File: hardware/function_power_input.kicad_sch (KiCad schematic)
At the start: 20 parts, among them J5 Conn_01x03_Socket, J6 Conn_01x03_Socket, U3 AZ1117-3.3

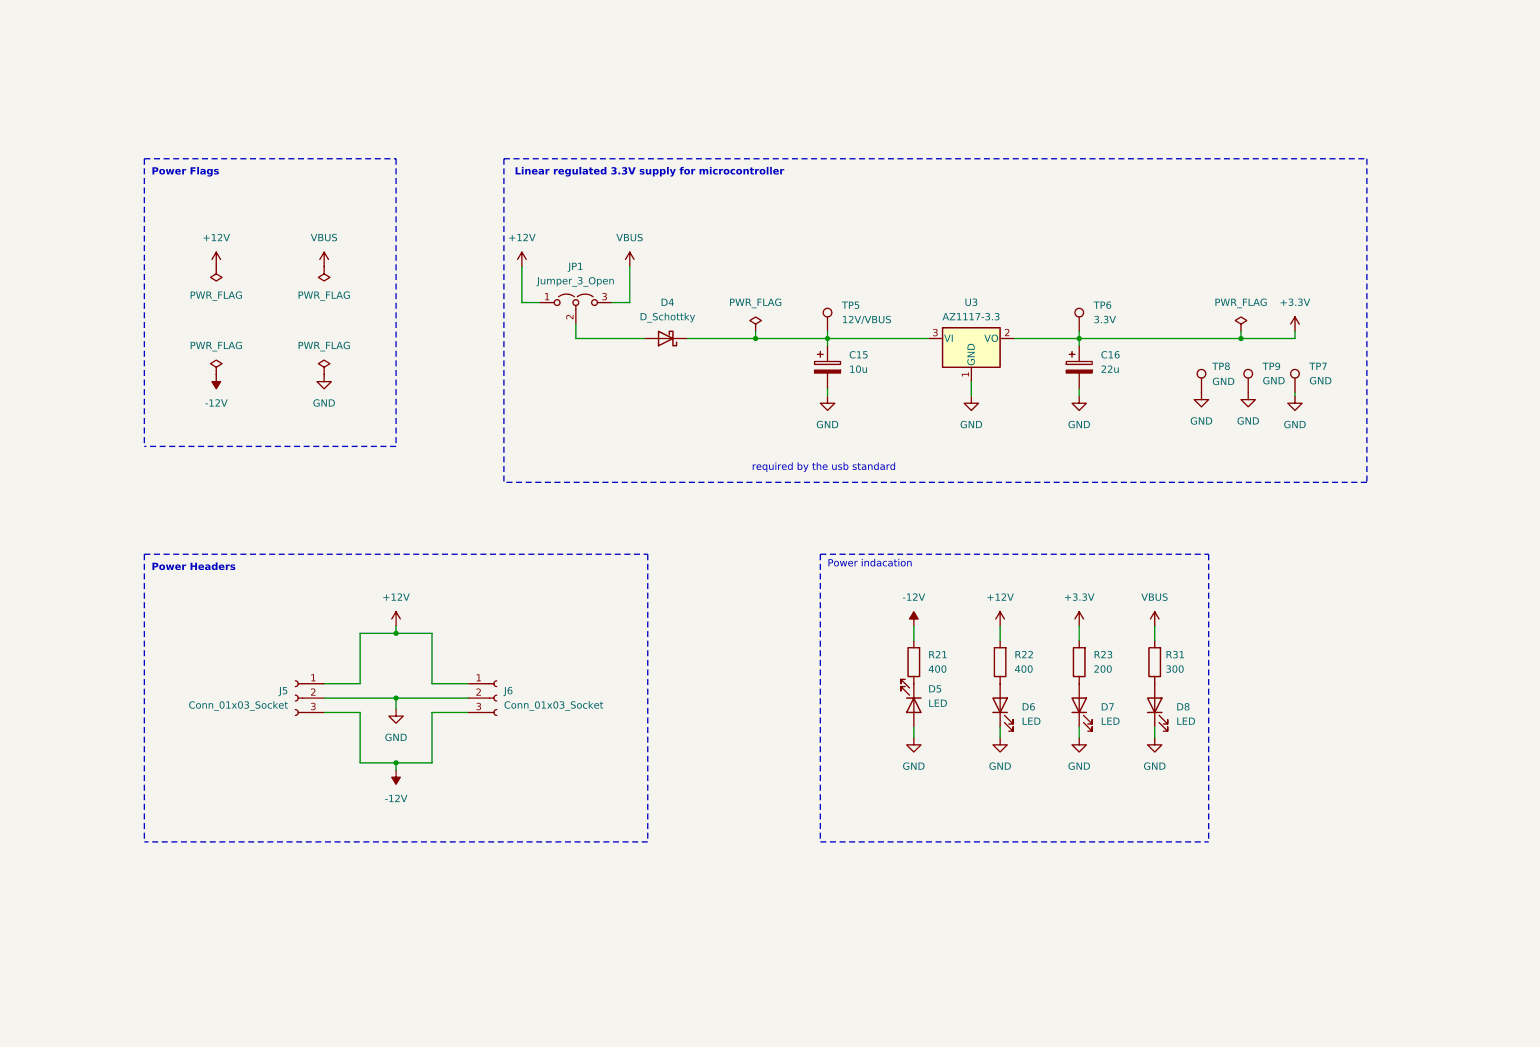
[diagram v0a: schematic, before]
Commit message: added a 5v reg for when RGB leds need powered from 12v
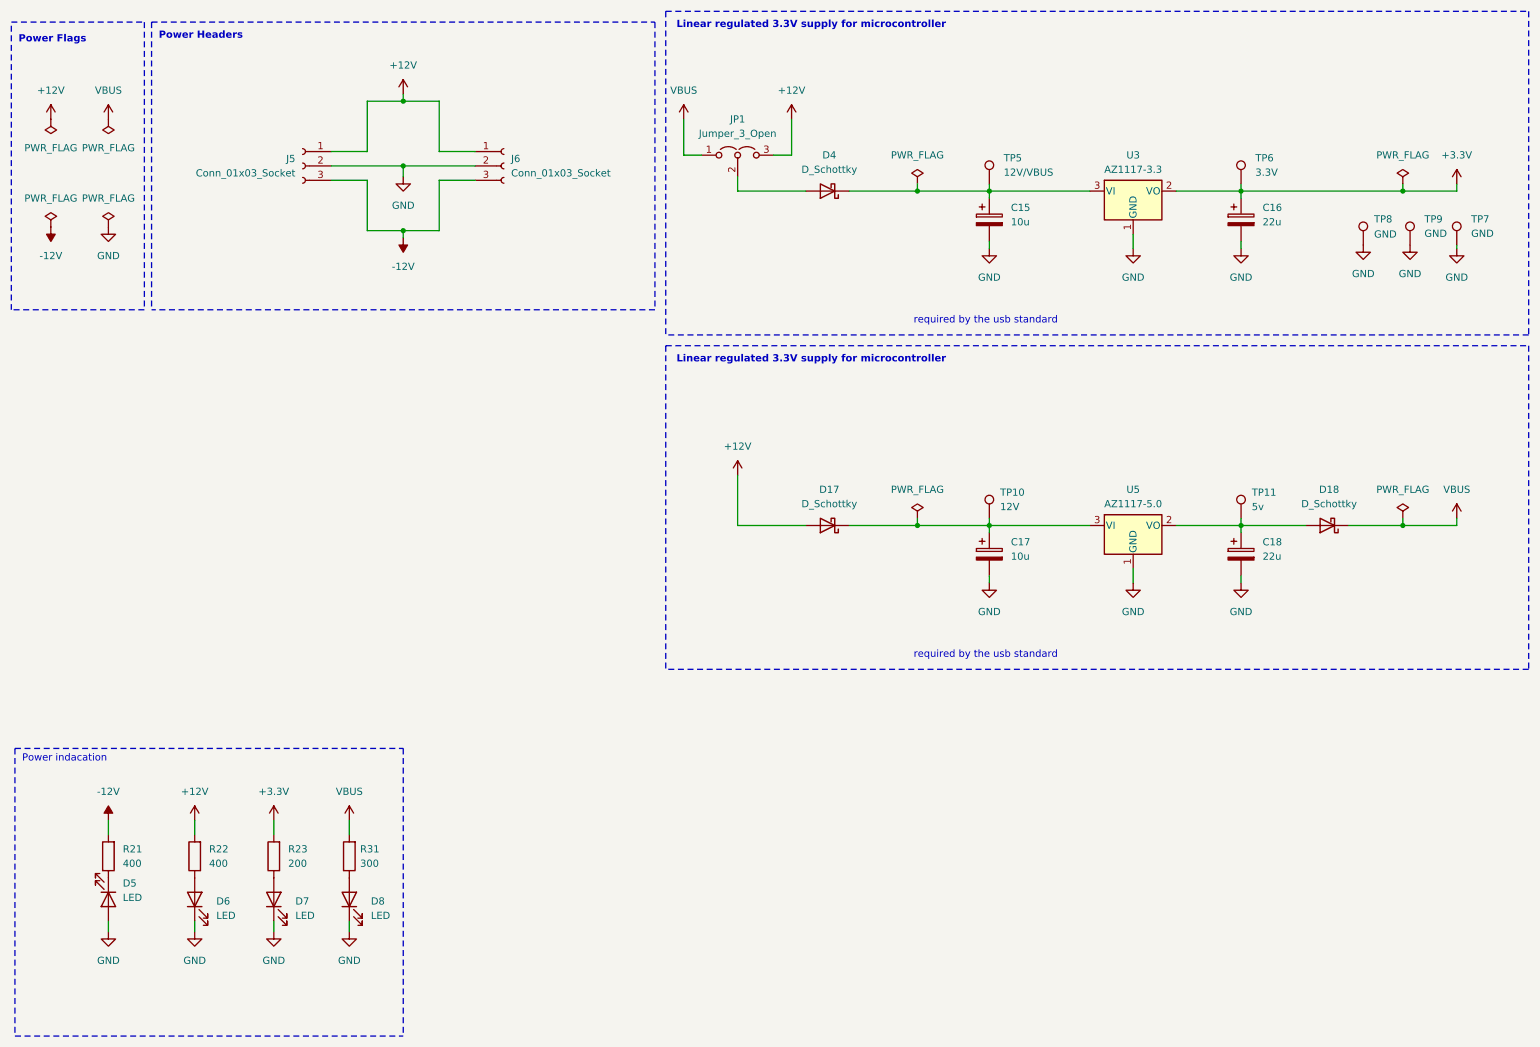
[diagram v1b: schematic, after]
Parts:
- added C17: 10u, Capacitor_SMD:C_0805_2012Metric, symbol Device:C_Polarized
- added C18: 22u, Capacitor_SMD:C_0805_2012Metric, symbol Device:C_Polarized
- added D17, D18: D_Schottky, Diode_SMD:D_0805_2012Metric, symbol Device:D_Schottky
- added TP10: 12V, TestPoint:TestPoint_Pad_D1.5mm, symbol Connector:TestPoint
- added TP11: 5v, TestPoint:TestPoint_Pad_D1.5mm, symbol Connector:TestPoint
- added U5: AZ1117-5.0, Package_TO_SOT_SMD:SOT-223, symbol Regulator_Linear:AZ1117-5.0
- JP1: footprint Connector_PinHeader_2.54mm:PinHeader_1x03_P2.54mm_Vertical -> Jumper:SolderJumper-3_P1.3mm_Bridged2Bar12_RoundedPad1.0x1.5mm_NumberLabels
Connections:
- net +12V: now also JP1.3 (B), D17.2 (A); no longer JP1.1 (A)
- net GND: now also C17.2, C18.2, U5.1 (GND)
- net VBUS: now also JP1.1 (A), D18.1 (K); no longer JP1.3 (B)
- new net: C18.1, D18.2 (A), TP11.1, U5.2 (VO)
- new net: C17.1, D17.1 (K), TP10.1, U5.3 (VI)
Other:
- moved on the sheet: C15, C16, D4, D5, D6, D7, D8, J5, J6, JP1, R21, R22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

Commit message: updated
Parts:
- added D22, D23, D24, D25: PTVS12VZ1USK, Diode_SMD:Nexperia_DSN1608-2_1.6x0.8mm, symbol Diode:PTVS12VZ1USK
- J5: footprint Connector_PinSocket_2.54mm:PinSocket_1x03_P2.54mm_Vertical -> Connector_PinHeader_2.54mm:PinHeader_1x03_P2.54mm_Horizontal
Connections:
- net +12V: now also D23.1 (K), D25.1 (K)
- net -12V: now also D22.2 (A), D24.2 (A)
- net GND: now also D22.1 (K), D23.2 (A), D24.1 (K), D25.2 (A)
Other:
- moved on the sheet: J5, J6
